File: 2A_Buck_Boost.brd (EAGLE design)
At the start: 25.4 x 20.3 mm, 42 parts, among them U1 TPS63070

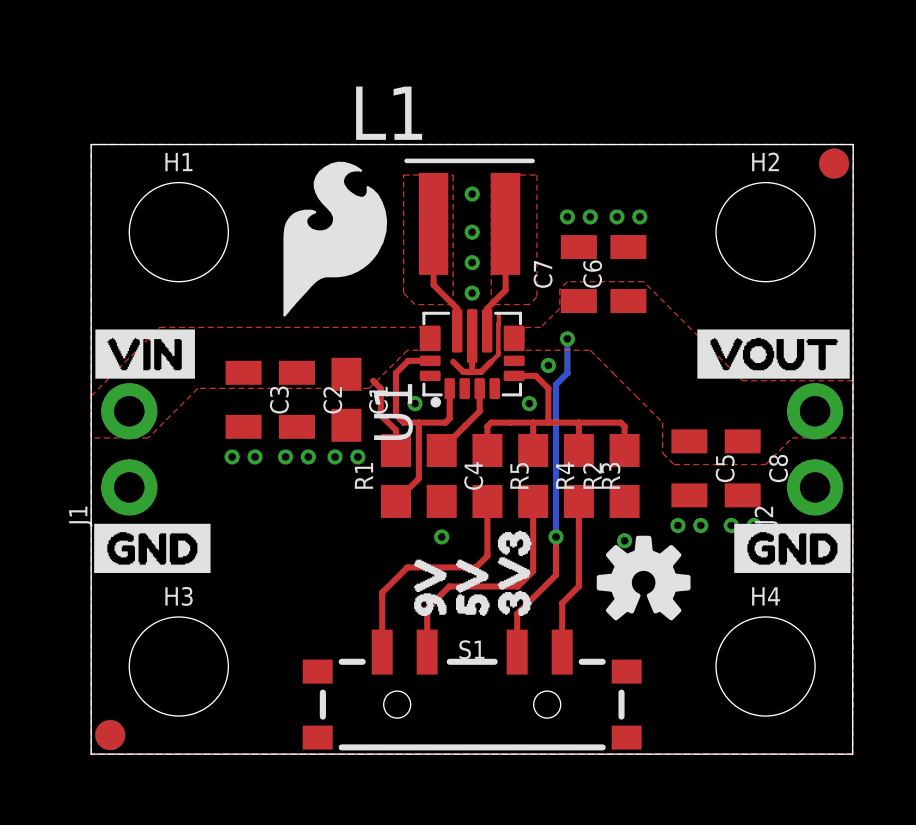
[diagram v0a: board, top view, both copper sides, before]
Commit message: Design Review Changes
-Moved standoffs 0.1" offset
-Added power LED with jumper to output
-Added vias under IC1
-Added units to measures layer
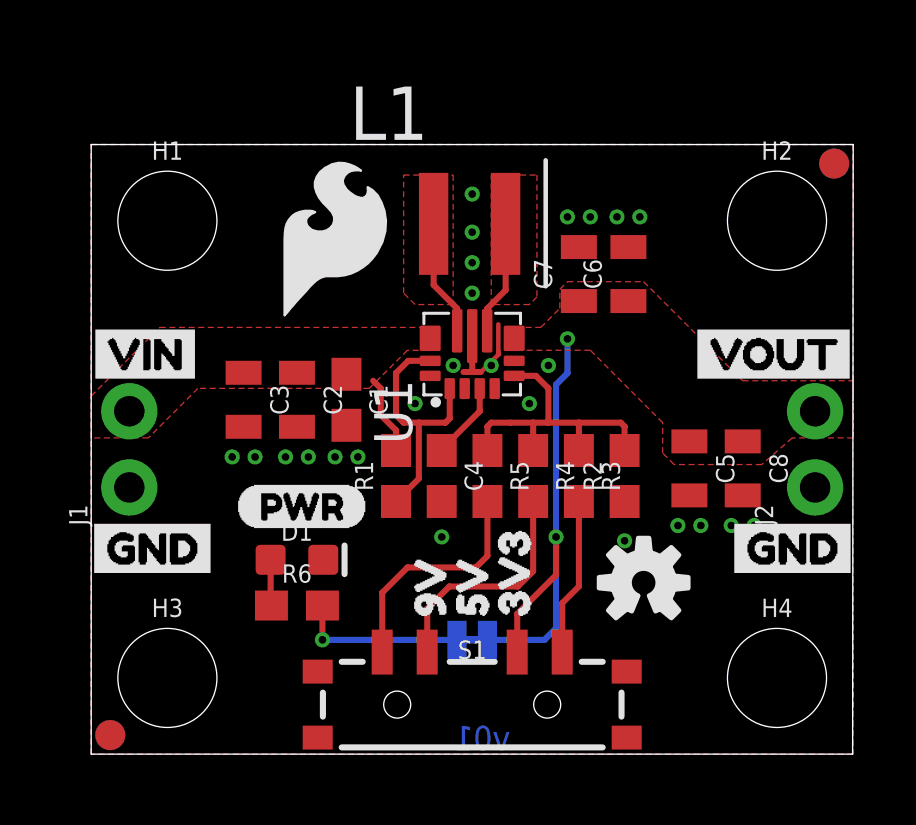
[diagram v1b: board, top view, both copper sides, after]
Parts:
- added D1: RED, SparkFun-LED:LED-0603
- added JP1: (no value), SparkFun-Jumpers:SMT-JUMPER_2_NC_TRACE_NO-SILK
- added R6: 1k, SparkFun-Resistors:0603
- added U$1: (no value), buzzard_labels:PWR2
- added U$11: (no value), buzzard_labels:PWR1
- added U$16: (no value), buzzard_labels:LED0
- U1: device SparkFun-IC-Power:15-VQFN-HR(3X2.5) -> SparkFun-IC-Power:VQFN-15-HR(3X2.5)
- moved FRAME1 13.1 mm to (-14.0, -16.5)
- moved U$15 3.05 mm to (18.8, 8.76)
- moved LOGO1 0.64 mm to (12.7, 14.4)
- moved H2 0.54 mm to (22.9, 17.8)
- moved H1 0.54 mm to (2.54, 17.8)
- moved H4 0.54 mm to (22.9, 2.54)
- moved H3 0.54 mm to (2.54, 2.54)
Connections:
- new net N$8: JP1.1, R6.2
- new net N$9: D1.A, R6.1
- net GND: now also D1.C
- net VOUT: now also JP1.2
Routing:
- net N$8: track 0.00 -> 5.63 mm, vias 0 -> 1
- net VOUT: track 11.1 -> 16.6 mm
- net N$9: track 0.00 -> 1.54 mm
- net GND: track 4.92 -> 3.63 mm, vias 23 -> 25
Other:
- board text added: "Alex Wende"
- board text added: "v01"

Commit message: QC Fixes
-Fixed board dimention width
-Fixed feedback resistor equation
-Adjusted power led silk
-Adjusted VIN copper pour to line up with C1 tstop
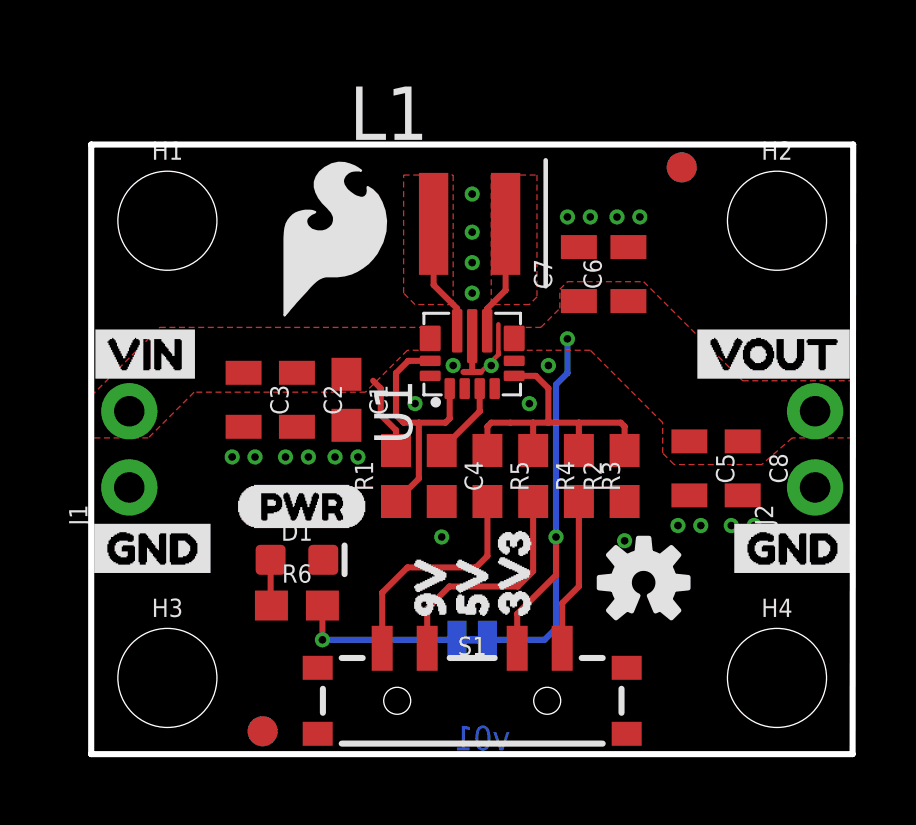
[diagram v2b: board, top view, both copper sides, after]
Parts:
- moved FD1 5.08 mm to (19.7, 19.6)
- moved FD2 5.08 mm to (19.7, 19.6)
- moved FD3 5.08 mm to (5.71, 0.76)
- moved FD4 5.08 mm to (5.71, 0.76)
- moved U$16 0.25 mm to (14.6, 2.29)
- moved U$11 0.13 mm to (14.9, 5.33)
- moved S1 0.13 mm to (12.7, 1.78)
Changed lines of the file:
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@@
 <layer number="27" name="tValues" color="7" fill="1" visible="no" active="yes"/>
 <layer number="28" name="bValues" color="7" fill="1" visible="no" active="yes"/>
-<layer number="29" name="tStop" color="7" fill="3" visible="no" active="yes"/>
+<layer number="29" name="tStop" color="7" fill="3" visible="yes" active="yes"/>
 <layer number="30" name="bStop" color="7" fill="6" visible="no" active="yes"/>
 <layer number="31" name="tCream" color="7" fill="4" visible="no" active="yes"/>
@@
 <board>
 <plain>
-<wire x1="0" y1="0" x2="25.38" y2="0" width="0.000203125" layer="20"/>
-<wire x1="25.38" y1="0" x2="25.4" y2="20.32" width="0.000203125" layer="20"/>
-<wire x1="25.4" y1="20.32" x2="0" y2="20.32" width="0.000203125" layer="20"/>
-<wire x1="0" y1="20.32" x2="0" y2="0" width="0.000203125" layer="20"/>
+<wire x1="0" y1="0" x2="25.38" y2="0" width="0.2032" layer="20"/>
+<wire x1="25.38" y1="0" x2="25.4" y2="20.32" width="0.2032" layer="20"/>
+<wire x1="25.4" y1="20.32" x2="0" y2="20.32" width="0.2032" layer="20"/>
+<wire x1="0" y1="20.32" x2="0" y2="0" width="0.2032" layer="20"/>
 <dimension x1="0" y1="0" x2="0" y2="20.32" x3="-5.08" y3="10.16" textsize="1.27" layer="47" unit="inch" precision="3"/>
 <dimension x1="0" y1="0" x2="25.4" y2="0" x3="12.7" y3="-5.08" textsize="1.27" layer="47" unit="inch" precision="3" visible="yes"/>
@@
 <attribute name="VALUE" x="26.162" y="7.62" size="0.6096" layer="27" font="vector" ratio="20" rot="R90"/>
 </element>
-<element name="S1" library="SparkFun-Switches" package="SWITCH_SP3T_SMD" value="" x="12.7" y="1.651" smashed="yes" rot="R180">
-<attribute name="NAME" x="12.7" y="3.175" size="0.6096" layer="25" font="vector" ratio="20" align="bottom-center"/>
-<attribute name="PROD_ID" value="SWCH-10805" x="12.7" y="1.651" size="1.778" layer="27" rot="R180" display="off"/>
-<attribute name="VALUE" x="12.7" y="0.127" size="0.6096" layer="27" font="vector" ratio="20" align="top-center"/>
+<element name="S1" library="SparkFun-Switches" package="SWITCH_SP3T_SMD" value="" x="12.7" y="1.778" smashed="yes" rot="R180">
+<attribute name="NAME" x="12.7" y="3.302" size="0.6096" layer="25" font="vector" ratio="20" align="bottom-center"/>
+<attribute name="PROD_ID" value="SWCH-10805" x="12.7" y="1.778" size="1.778" layer="27" rot="R180" display="off"/>
+<attribute name="VALUE" x="12.7" y="0.254" size="0.6096" layer="27" font="vector" ratio="20" align="top-center"/>
 </element>
 <element name="R3" library="SparkFun-Resistors" package="0603" value="213k" x="16.256" y="9.271" smashed="yes" rot="R270">
@@
 <attribute name="VALUE" x="22.86" y="15.748" size="0.6096" layer="27" font="vector" ratio="20" align="top-center"/>
 </element>
-<element name="FD3" library="SparkFun-Aesthetics" package="FIDUCIAL-1X2" value="FIDUCIAL1X2" x="0.635" y="0.635" smashed="yes"/>
-<element name="FD4" library="SparkFun-Aesthetics" package="FIDUCIAL-1X2" value="FIDUCIAL1X2" x="0.635" y="0.635" smashed="yes" rot="MR0"/>
-<element name="FD1" library="SparkFun-Aesthetics" package="FIDUCIAL-1X2" value="FIDUCIAL1X2" x="24.765" y="19.685" smashed="yes"/>
-<element name="FD2" library="SparkFun-Aesthetics" package="FIDUCIAL-1X2" value="FIDUCIAL1X2" x="24.765" y="19.685" smashed="yes" rot="MR0"/>
+<element name="FD3" library="SparkFun-Aesthetics" package="FIDUCIAL-1X2" value="FIDUCIAL1X2" x="5.715" y="0.762" smashed="yes"/>
+<element name="FD4" library="SparkFun-Aesthetics" package="FIDUCIAL-1X2" value="FIDUCIAL1X2" x="5.715" y="0.762" smashed="yes" rot="MR0"/>
+<element name="FD1" library="SparkFun-Aesthetics" package="FIDUCIAL-1X2" value="FIDUCIAL1X2" x="19.685" y="19.558" smashed="yes"/>
+<element name="FD2" library="SparkFun-Aesthetics" package="FIDUCIAL-1X2" value="FIDUCIAL1X2" x="19.685" y="19.558" smashed="yes" rot="MR0"/>
 <element name="U$9" library="SparkFun-Aesthetics" package="SFE_LOGO_FLAME_.2" value="" x="8.128" y="17.145" smashed="yes"/>
 <element name="U$5" library="buzzard_labels" package="VIN3" value="" x="-0.381" y="13.335" smashed="yes"/>
@@
 <element name="JP1" library="SparkFun-Jumpers" package="SMT-JUMPER_2_NC_TRACE_NO-SILK" value="" x="12.7" y="3.81" rot="MR180"/>
 <element name="U$1" library="buzzard_labels" package="PWR2" value="" x="4.826" y="8.255"/>
-<element name="U$11" library="buzzard_labels" package="PWR1" value="" x="14.986" y="5.334" rot="MR0"/>
-<element name="U$16" library="buzzard_labels" package="LED0" value="" x="14.859" y="2.286" rot="MR0"/>
+<element name="U$11" library="buzzard_labels" package="PWR1" value="" x="14.859" y="5.334" rot="MR0"/>
+<element name="U$16" library="buzzard_labels" package="LED0" value="" x="14.605" y="2.286" rot="MR0"/>
 </elements>
 <signals>
@@
 <vertex x="11.557" y="13.462"/>
 <vertex x="10.541" y="13.462"/>
-<vertex x="9.271" y="12.192"/>
-<vertex x="3.556" y="12.192"/>
+<vertex x="9.144" y="12.065"/>
+<vertex x="3.429" y="12.065"/>
 <vertex x="1.905" y="10.541"/>
 <vertex x="0" y="10.541"/>
@@
 <via x="15.494" y="7.239" extent="1-16" drill="0.254"/>
 <via x="15.875" y="13.843" extent="1-16" drill="0.254"/>
-<wire x1="14.2" y1="3.401" x2="14.2" y2="4.675" width="0.2032" layer="1"/>
+<wire x1="14.2" y1="3.528" x2="14.2" y2="4.675" width="0.2032" layer="1"/>
 <wire x1="14.2" y1="4.675" x2="15.494" y2="5.969" width="0.2032" layer="1"/>
 <wire x1="15.494" y1="5.969" x2="15.494" y2="7.239" width="0.2032" layer="1"/>
@@
 <wire x1="13.208" y1="6.604" x2="12.827" y2="6.223" width="0.2032" layer="1"/>
 <wire x1="12.827" y1="6.223" x2="10.541" y2="6.223" width="0.2032" layer="1"/>
-<wire x1="9.7" y1="5.382" x2="9.7" y2="3.401" width="0.2032" layer="1"/>
+<wire x1="9.7" y1="5.382" x2="9.7" y2="3.528" width="0.2032" layer="1"/>
 <wire x1="10.541" y1="6.223" x2="9.7" y2="5.382" width="0.2032" layer="1"/>
 </signal>
@@
 <wire x1="14.224" y1="5.588" x2="11.938" y2="5.588" width="0.2032" layer="1"/>
 <wire x1="11.938" y1="5.588" x2="11.2" y2="4.85" width="0.2032" layer="1"/>
-<wire x1="11.2" y1="4.85" x2="11.2" y2="3.401" width="0.2032" layer="1"/>
+<wire x1="11.2" y1="4.85" x2="11.2" y2="3.528" width="0.2032" layer="1"/>
 </signal>
 <signal name="N$7">
@@
 <contactref element="R3" pad="2"/>
 <wire x1="16.256" y1="8.421" x2="16.256" y2="5.588" width="0.2032" layer="1"/>
-<wire x1="15.7" y1="5.032" x2="15.7" y2="3.401" width="0.2032" layer="1"/>
+<wire x1="15.7" y1="5.032" x2="15.7" y2="3.528" width="0.2032" layer="1"/>
 <wire x1="16.256" y1="5.588" x2="15.7" y2="5.032" width="0.2032" layer="1"/>
 </signal>
